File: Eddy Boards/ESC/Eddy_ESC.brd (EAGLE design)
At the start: 101.6 x 101.6 mm, 10 parts

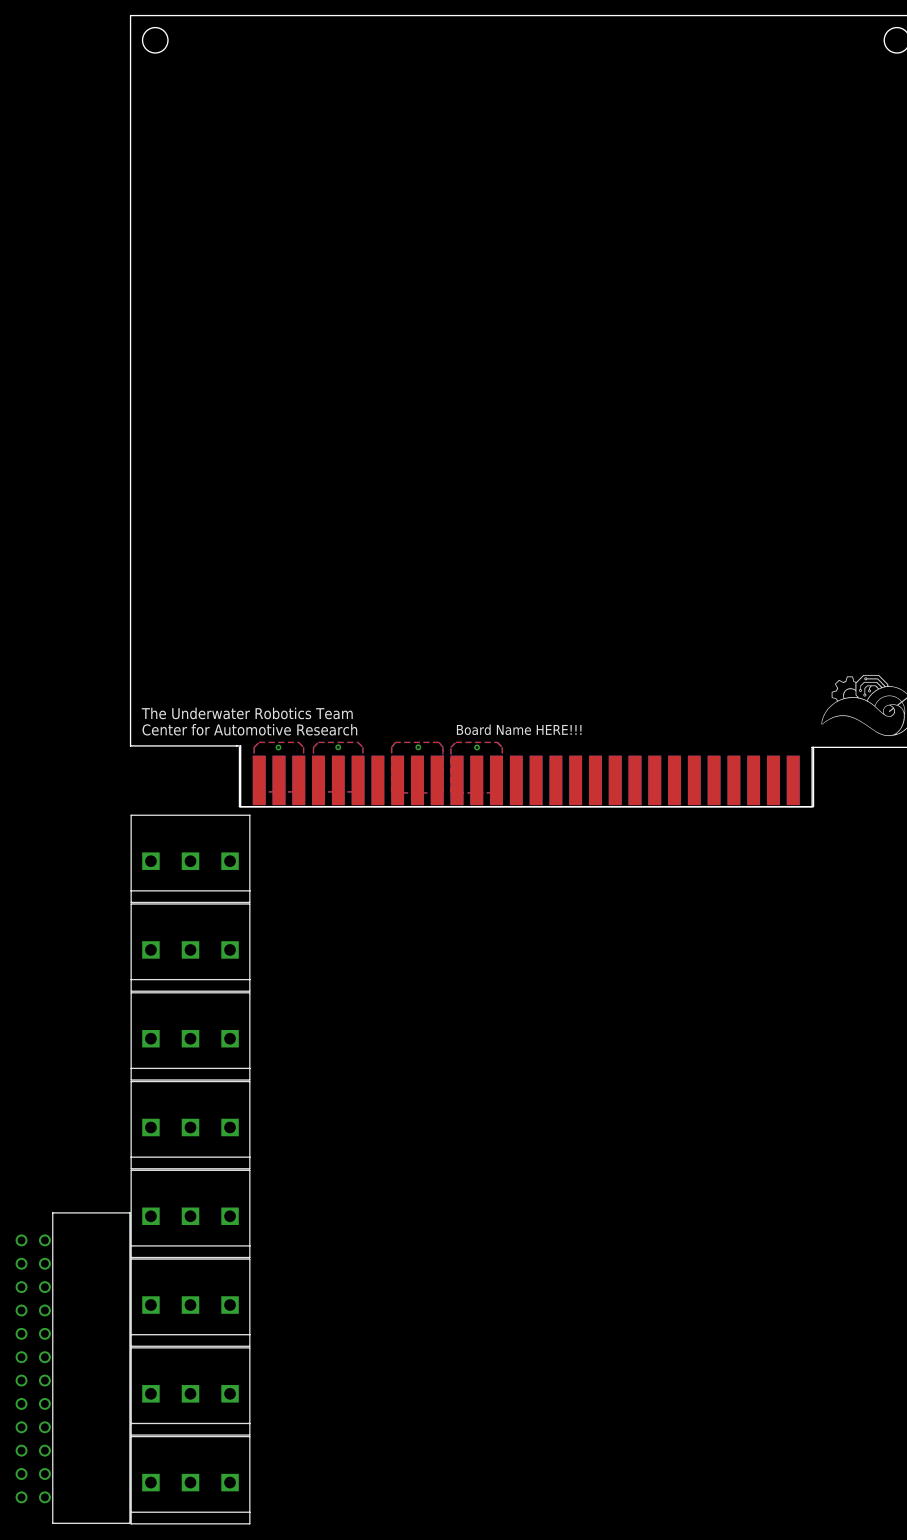
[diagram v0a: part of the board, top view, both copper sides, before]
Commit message: addded PWM's to connector and adjusted positioning
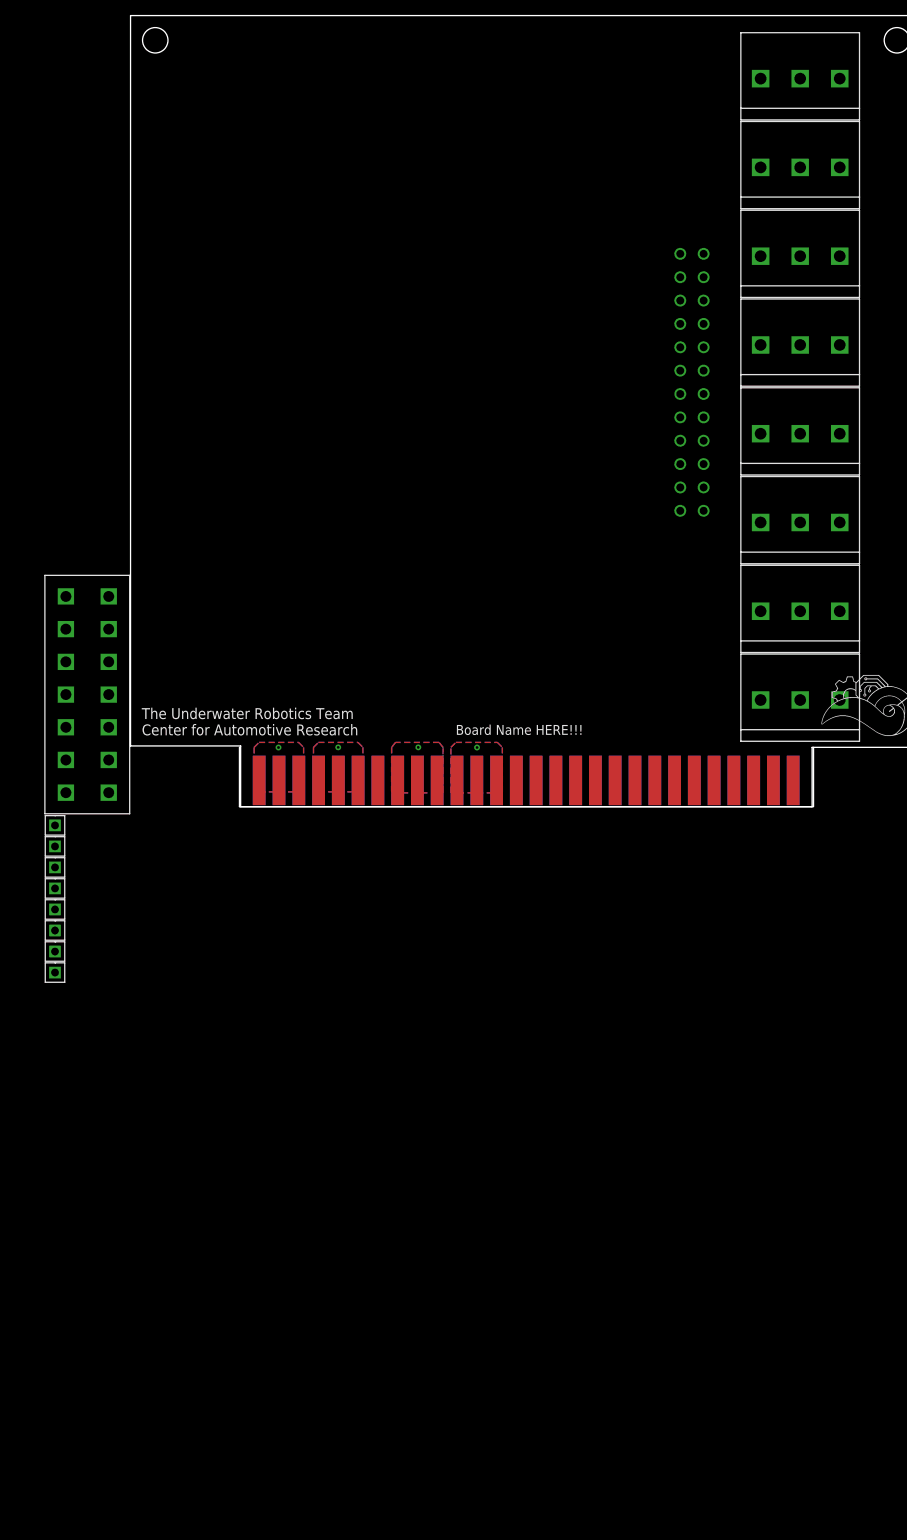
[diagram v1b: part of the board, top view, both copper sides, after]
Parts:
- added U$11: 14PIN_VERT, 14_Pin_Connector_Vert:14PIN_VERT
- added U$12, U$13, U$14, U$15, U$16, U$17, U$18, U$19: MALE1PINHEADER, Male_Header_1Pin:MALE1PINHEADER
- moved U$10 154.0 mm to (73.6, 38.0), flipped to the bottom
- moved U$2 127.4 mm to (86.0, 93.5)
- moved U$3 127.4 mm to (86.0, 82.1)
- moved U$4 127.4 mm to (86.0, 70.7)
- moved U$5 127.4 mm to (86.0, 59.3)
- moved U$6 127.4 mm to (86.0, 47.9)
- moved U$7 127.4 mm to (86.0, 36.5)
- moved U$8 127.4 mm to (86.0, 25.1)
- moved U$9 127.4 mm to (86.0, 13.7)
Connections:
- new net N$25: U$1.20, U$12.PWM
- new net N$26: U$1.21, U$13.PWM
- new net N$27: U$1.22, U$14.PWM
- new net N$28: U$1.23, U$16.PWM
- new net N$29: U$1.24, U$15.PWM
- new net N$30: U$1.25, U$17.PWM
- new net N$31: U$1.26, U$18.PWM
- new net N$32: U$1.27, U$19.PWM
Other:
- outline, holes or cut-outs redrawn

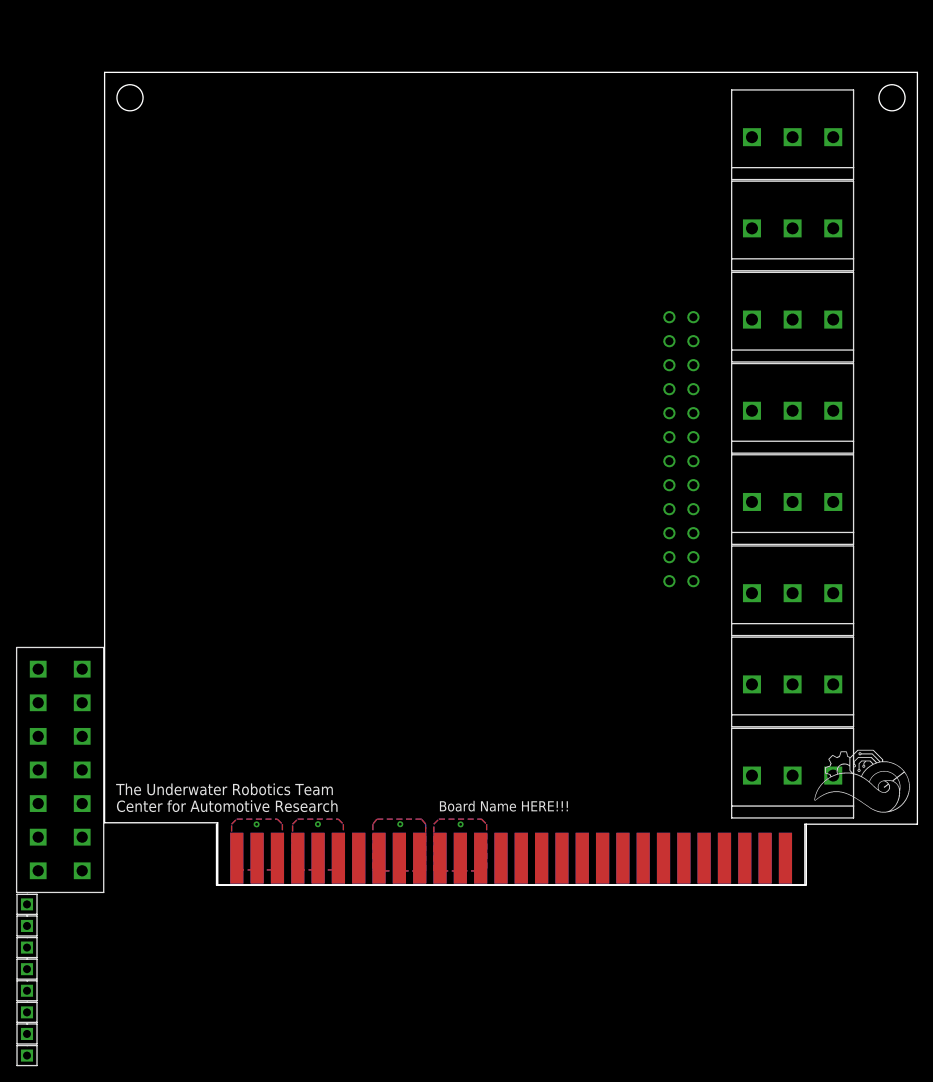
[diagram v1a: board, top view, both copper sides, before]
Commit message: added LED
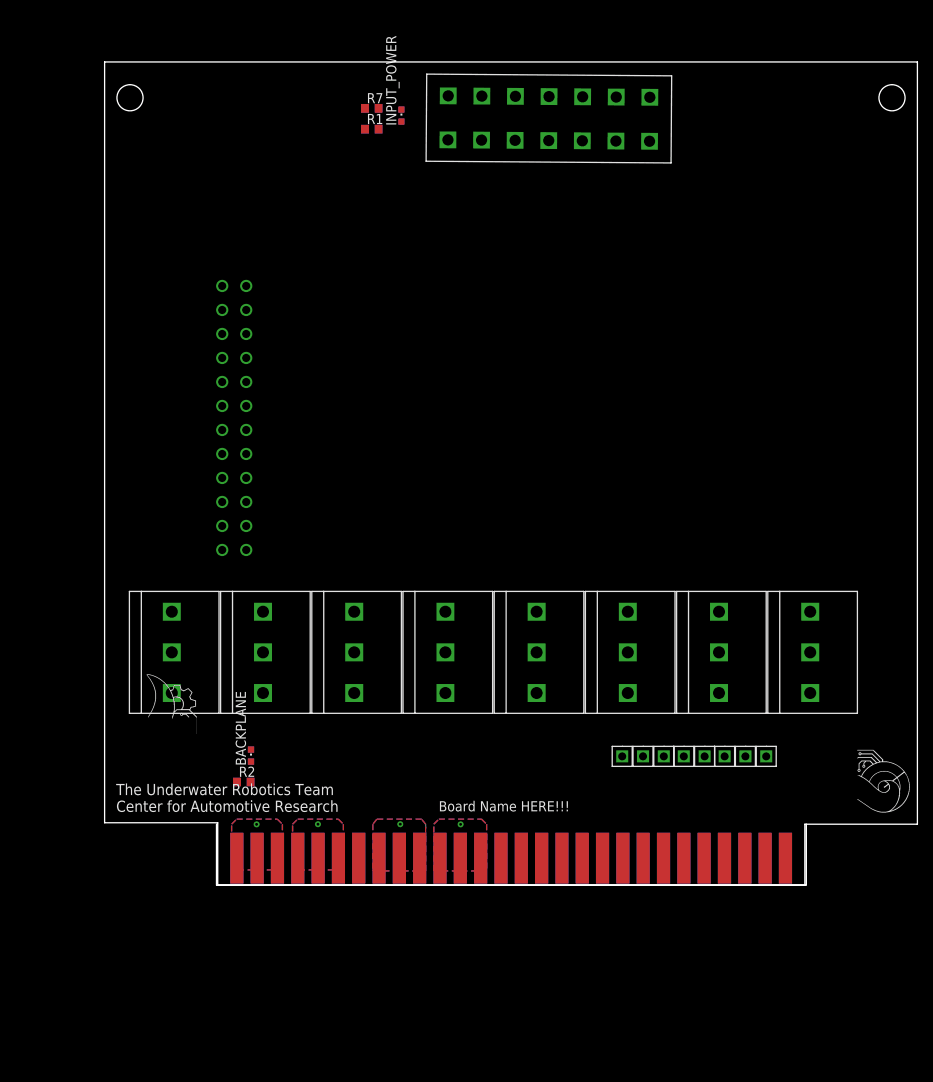
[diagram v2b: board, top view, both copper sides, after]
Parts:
- added BACKPLANE, INPUT_POWER: (no value), led:CHIPLED_0603
- added R1, R7: 900, resistor:R0603
- added R2: 5, resistor:R0603
- moved U$11 109.6 mm to (43.0, 98.7), turned to 269.6 degrees
- moved U$19 99.7 mm to (82.7, 16.1)
- moved U$18 96.3 mm to (80.1, 16.1)
- moved U$17 92.9 mm to (77.5, 16.1)
- moved U$15 88.8 mm to (75.0, 16.1)
- moved U$16 87.2 mm to (72.4, 16.1)
- moved U$14 83.1 mm to (69.9, 16.1)
- moved U$13 79.9 mm to (67.3, 16.1)
- moved U$9 79.1 mm to (8.40, 29.1), turned to 270 degrees
- moved U$12 76.7 mm to (64.7, 16.1)
- moved U$8 66.3 mm to (19.8, 29.1), turned to 270 degrees
- moved U$2 64.4 mm to (88.2, 29.1), turned to 270 degrees
- moved U$10 56.0 mm to (17.7, 41.9)
- moved U$7 55.3 mm to (31.2, 29.1), turned to 270 degrees
- moved U$3 53.8 mm to (76.8, 29.1), turned to 270 degrees
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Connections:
- new net N$33: INPUT_POWER.A, R1.2, R7.2
- new net N$34: BACKPLANE.A, R2.2
- new net N$39: R1.1, R7.1, U$11.1+, U$11.2+, U$11.3+, U$11.4+, U$11.5+, U$11.6+, U$11.7+
- new net N$44: U$11.3-
- net +3V3: now also R2.1
- net GND: now also BACKPLANE.C, INPUT_POWER.C, U$11.1-, U$11.2-, U$11.4-, U$11.5-, U$11.6-, U$11.7-
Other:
- board size 101.6 x 101.6 mm -> 101.6 x 102.9 mm

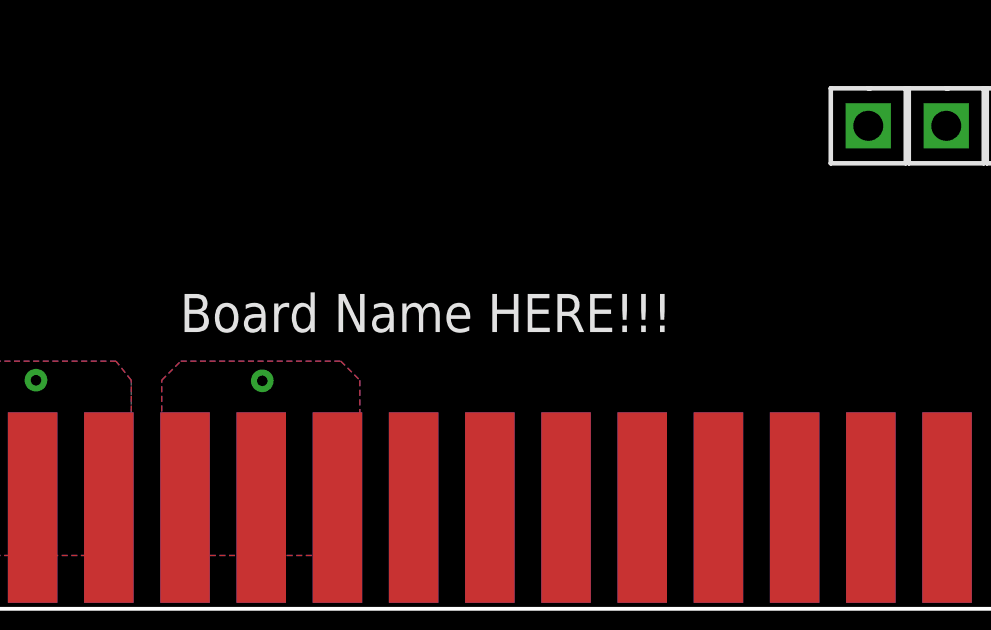
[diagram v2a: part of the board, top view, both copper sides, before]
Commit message: finished sheet 1, moved items on board around- will add labels to sheet 1 later
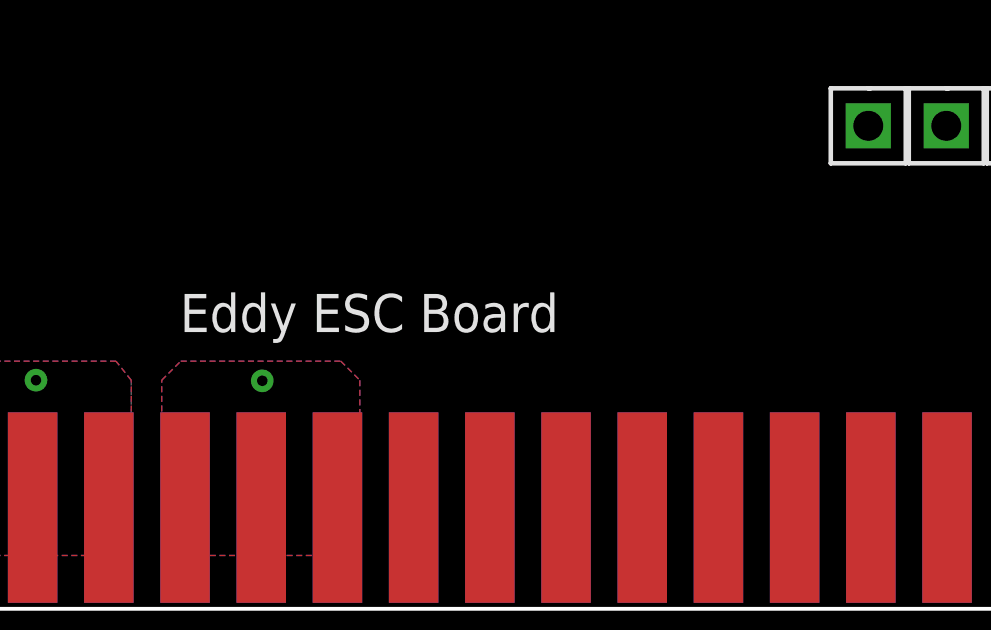
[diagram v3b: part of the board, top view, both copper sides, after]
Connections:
- new net N$35: U$1.32
- new net N$36: U$1.31
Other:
- board text added: "Eddy ESC Board"
- board text removed: "Board Name HERE!!!"
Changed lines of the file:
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@@
 <rectangle x1="94.09175625" y1="16.875759375" x2="96.144075" y2="16.896078125" layer="21"/>
 <rectangle x1="94.112078125" y1="16.896078125" x2="96.123753125" y2="16.916396875" layer="21"/>
-<text x="41.757603125" y="9.225278125" size="1.27" layer="21">Board Name HERE!!!</text>
+<text x="41.757603125" y="9.225278125" size="1.27" layer="21">Eddy ESC Board</text>
 <text x="1.44271875" y="9.16431875" size="1.397" layer="21" ratio="4">The Underwater Robotics Team
 Center for Automotive Research</text>
@@
 <wire x1="47.116409375" y1="93.132421875" x2="55.516203125" y2="93.073778125" width="0" layer="19" extent="1-1"/>
 <wire x1="42.916509375" y1="93.161740625" x2="47.116409375" y2="93.132421875" width="0" layer="19" extent="1-1"/>
-<wire x1="36.957" y1="7.62" x2="42.916509375" y2="93.161740625" width="0" layer="19" extent="1-1"/>
-<wire x1="36.8455" y1="3.375" x2="36.957" y2="7.62" width="0" layer="19" extent="16-16"/>
-<wire x1="26.67" y1="7.62" x2="26.6855" y2="3.375" width="0" layer="19" extent="16-16"/>
-<wire x1="37.1" y1="96.95" x2="24.1455" y2="3.375" width="0" layer="19" extent="1-16"/>
-<wire x1="18.3" y1="16.95" x2="37.1" y2="96.95" width="0" layer="19" extent="1-1"/>
+<wire x1="37.1" y1="96.95" x2="42.916509375" y2="93.161740625" width="0" layer="19" extent="1-1"/>
+<wire x1="18.3" y1="16.95" x2="42.916509375" y2="93.161740625" width="0" layer="19" extent="1-1"/>
+<wire x1="26.67" y1="7.62" x2="18.3" y2="16.95" width="0" layer="19" extent="1-1"/>
+<wire x1="26.6855" y1="3.375" x2="26.67" y2="7.62" width="0" layer="19" extent="16-16"/>
+<wire x1="36.957" y1="7.62" x2="36.8455" y2="3.375" width="0" layer="19" extent="16-16"/>
 </signal>
 <signal name="+5V">
@@
 </polygon>
 <via x="44.5" y="7.6" extent="1-16" drill="0.35"/>
+<wire x1="44.4655" y1="3.375" x2="44.5" y2="7.6" width="0" layer="19" extent="16-16"/>
 </signal>
 <signal name="+3V3">
@@
 <via x="19" y="7.6" extent="1-16" drill="0.35"/>
 <contactref element="R2" pad="1"/>
+<wire x1="19" y1="7.6" x2="16.55" y2="12.9" width="0" layer="19" extent="1-1"/>
 <wire x1="19.0655" y1="3.375" x2="19" y2="7.6" width="0" layer="19" extent="16-16"/>
-<wire x1="16.55" y1="12.9" x2="16.5255" y2="3.375" width="0" layer="19" extent="1-1"/>
 </signal>
 <signal name="N$1">
@@
 <wire x1="18.25" y1="12.9" x2="18.3" y2="15.45" width="0" layer="19" extent="1-1"/>
 </signal>
+<signal name="N$35">
+<contactref element="U$1" pad="32"/>
+</signal>
+<signal name="N$36">
+<contactref element="U$1" pad="31"/>
+</signal>
 </signals>
